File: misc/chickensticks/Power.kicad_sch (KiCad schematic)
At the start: 26 parts, among them J10 Conn_01x03_Pin, Q1 Si2371EDS, Q2 DMG9926UDM, U5 LP5907MFX-3.3, U6 MCP73831-2-MC, U7 BQ29700

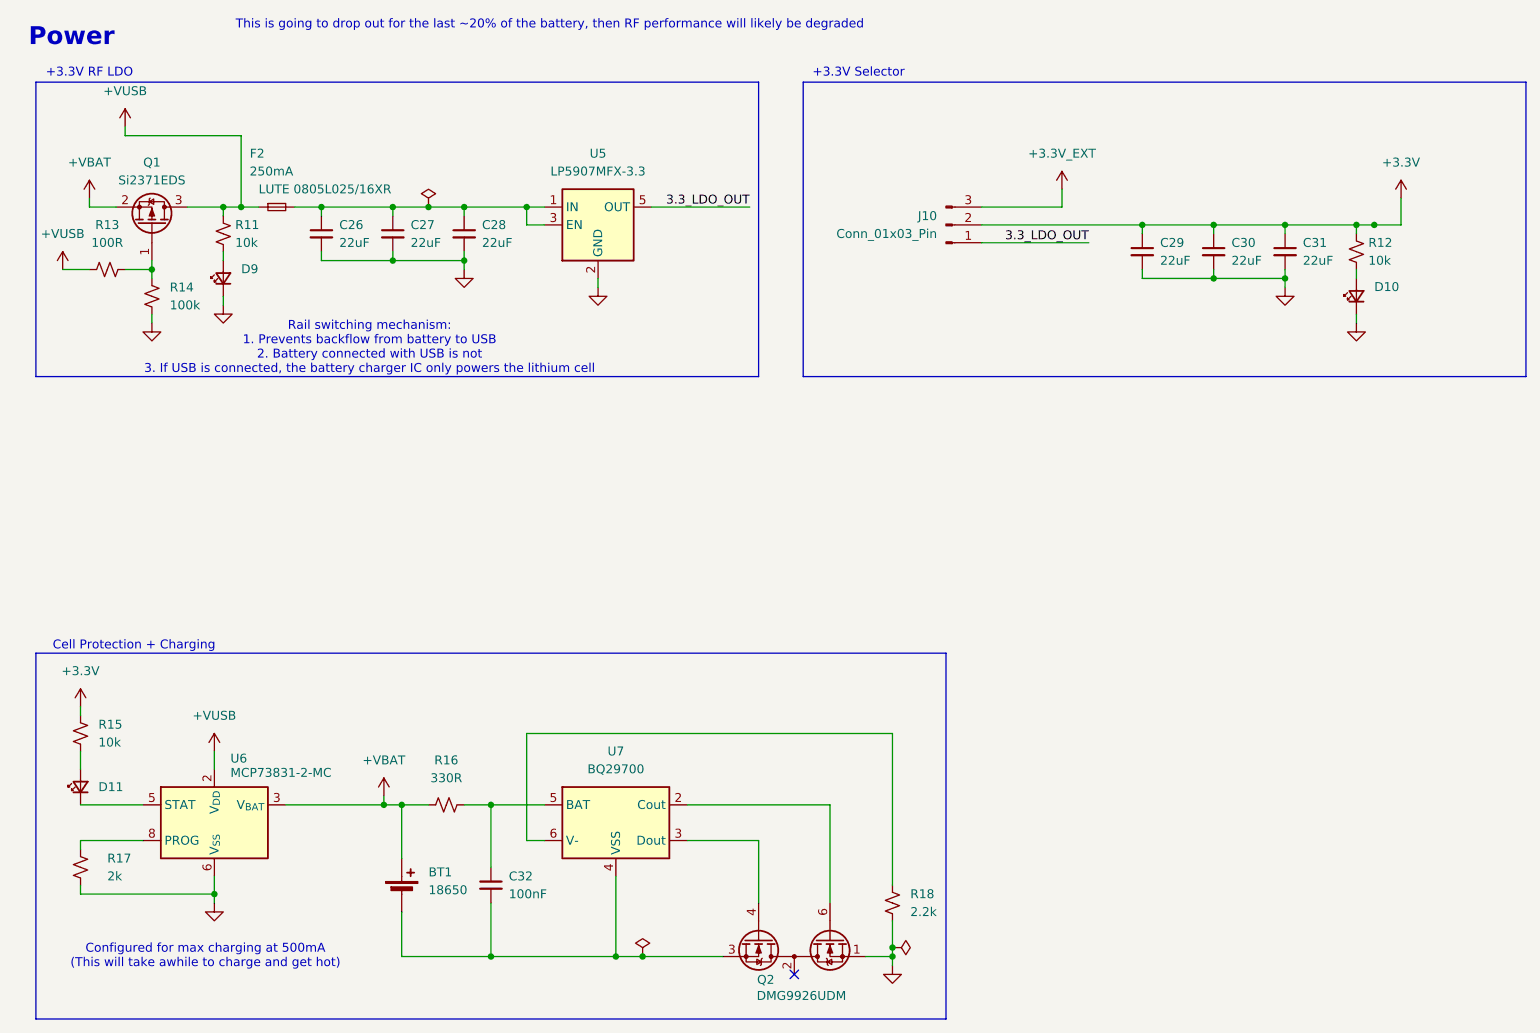
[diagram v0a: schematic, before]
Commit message: the great flatpak and kicad 10.0.6 migration
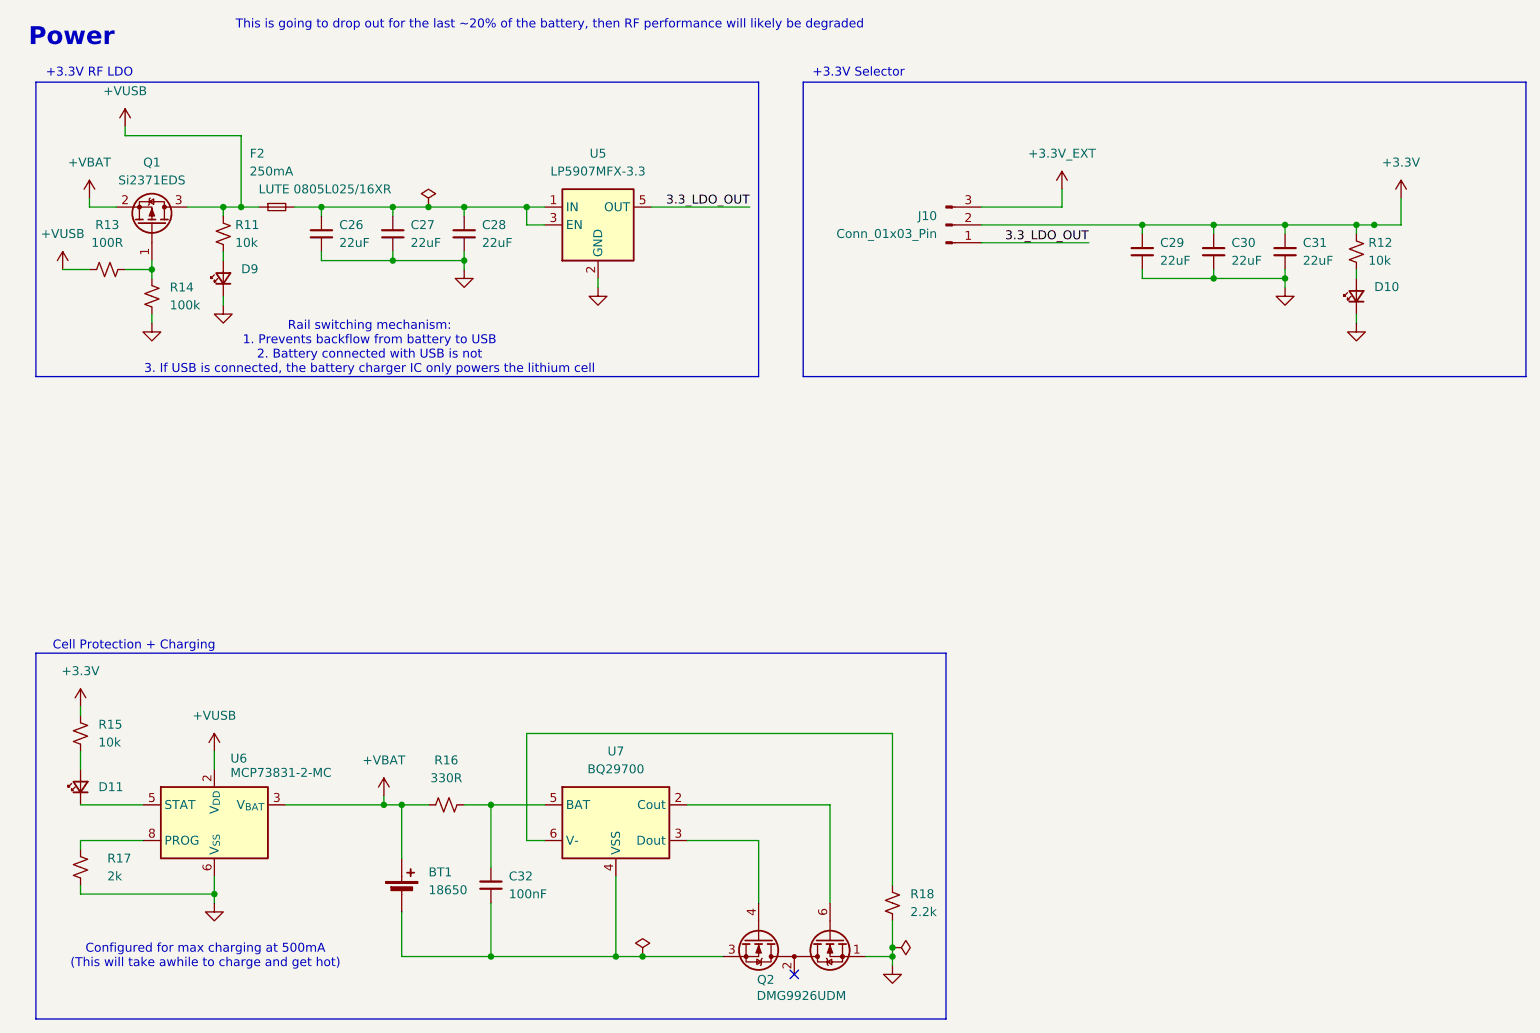
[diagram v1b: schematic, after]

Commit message: Document setup, update template, and use an ampersand when referring to APRL
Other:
- company: Aggie Propulsion and Rocketry Lab -> Aggie Propulsion & Rocketry Lab
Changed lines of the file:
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@@
 		(title "Chickenstick")
 		(rev "0")
-		(company "Aggie Propulsion and Rocketry Lab")
+		(company "Aggie Propulsion & Rocketry Lab")
 		(comment 1 "Drawn by: Nolan Poe")
 		(comment 2 "Reviewed by: Daniel Fan (and hopefully Tim Solberg)")
